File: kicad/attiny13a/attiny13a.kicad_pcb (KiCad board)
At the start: 2 copper layers, 28.2 x 17.8 mm, 6 parts, among them P1 CONN_01X04, P2 CONN_01X04, P3 CONN_01X06, U1 ATTINY13A-SSU

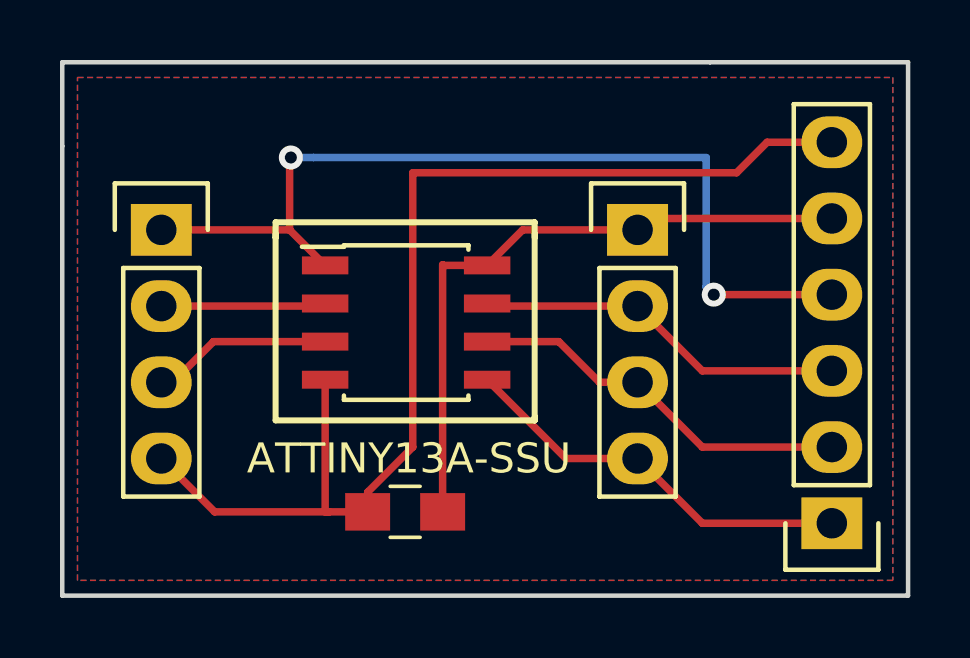
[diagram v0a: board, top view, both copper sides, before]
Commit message: make a better pcb
included sabor suggestions

1. Change vcc copper fill to GND fill
2. remove gnd traces
3. redraw vcc traces
4. move bypass capacitor close to Vcc/GND as much as possible.

Signed-off-by: Amitesh Singh <singh.amitesh@gmail.com>
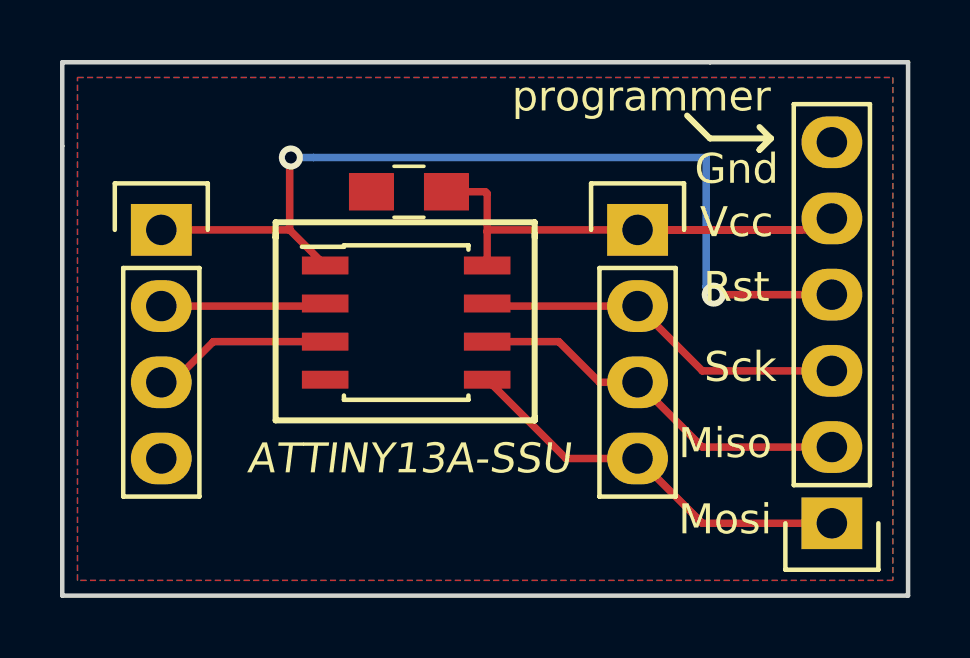
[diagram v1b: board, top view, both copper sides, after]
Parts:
- moved C1 10.7 mm to (131.2, 87.9)
- moved G*** 5.94 mm to (129.3, 96.5)
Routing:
- net GND: track 38.5 -> 0.00 mm
- net VCC: track 21.9 -> 20.9 mm
- added copper zone on F.Cu, net GND
- removed copper zone on F.Cu, net VCC
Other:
- board text added: "Gnd"
- board text added: "Miso"
- board text added: "Mosi"
- board text added: "Rst"
- board text added: "Sck"
- board text added: "Vcc"
- board text added: "programmer"

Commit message: change name to ISP
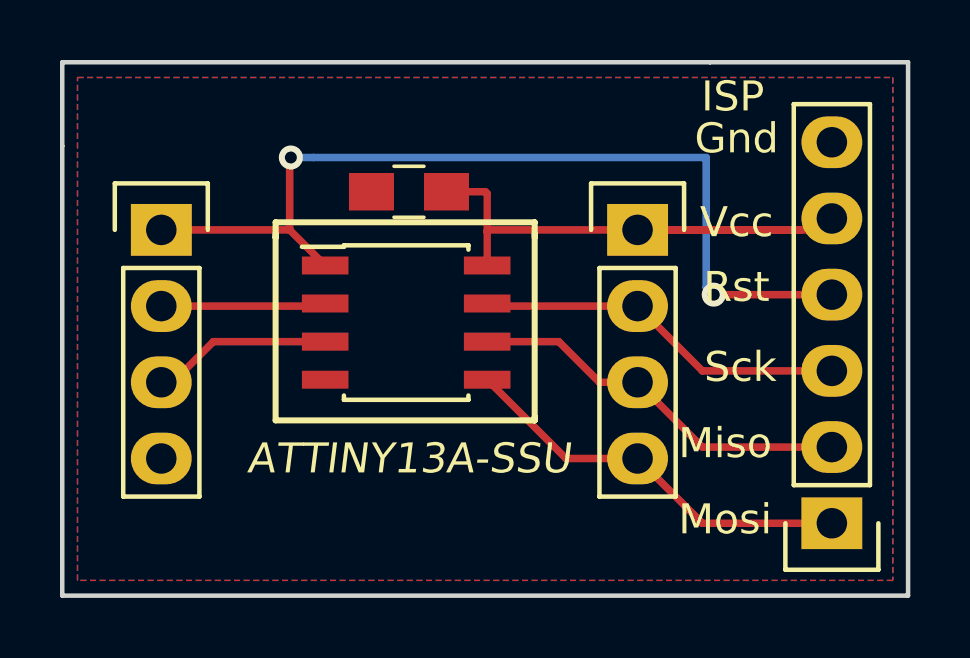
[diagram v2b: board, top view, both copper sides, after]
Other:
- board text added: "ISP"
- board text removed: "programmer"
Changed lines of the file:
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@@
     (links 16)
     (no_connects 0)
-    (area 119.558999 83.490999 147.903001 101.421001)
+    (area 119.558999 83.490999 149.8095 101.421001)
     (thickness 1.6)
-    (drawings 27)
+    (drawings 21)
     (tracks 38)
     (zones 0)
@@
       (effects (font (size 1 1) (thickness 0.15)))
     )
-    (fp_text value CONN_01X04 (at -1.905 2.413 360) (layer F.Fab) hide
+    (fp_text value CONN_01X04 (at -1.905 2.413) (layer F.Fab) hide
       (effects (font (size 1 1) (thickness 0.15)))
     )
@@
       (xy 4.318 -3.386667)) (layer B.SilkS) (width 0.01))
   )
-  (gr_text Gnd (at 142.113 87.122) (layer F.SilkS)
+  (gr_text Gnd (at 142.113 86.106) (layer F.SilkS)
     (effects (font (size 1 1) (thickness 0.2)))
   )
@@
     (effects (font (size 1 1) (thickness 0.2)))
   )
-  (gr_line (start 143.256 86.106) (end 142.875 85.725) (angle 90) (layer F.SilkS) (width 0.2))
-  (gr_line (start 142.875 86.487) (end 143.256 86.106) (angle 90) (layer F.SilkS) (width 0.2))
-  (gr_line (start 143.256 86.106) (end 142.875 86.487) (angle 90) (layer F.SilkS) (width 0.2))
-  (gr_line (start 143.129 86.106) (end 143.256 86.106) (angle 90) (layer F.SilkS) (width 0.2))
-  (gr_line (start 141.224 86.106) (end 143.129 86.106) (angle 90) (layer F.SilkS) (width 0.2))
-  (gr_line (start 140.462 85.344) (end 141.224 86.106) (angle 90) (layer F.SilkS) (width 0.2))
-  (gr_text programmer (at 138.938 84.709) (layer F.SilkS)
-    (effects (font (size 1 1) (thickness 0.2)))
-  )
+  (gr_text ISP (at 141.986 84.709) (layer F.SilkS)
+    (effects (font (size 1 1) (thickness 0.2)))
+  )

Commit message: make vcc track size bigger
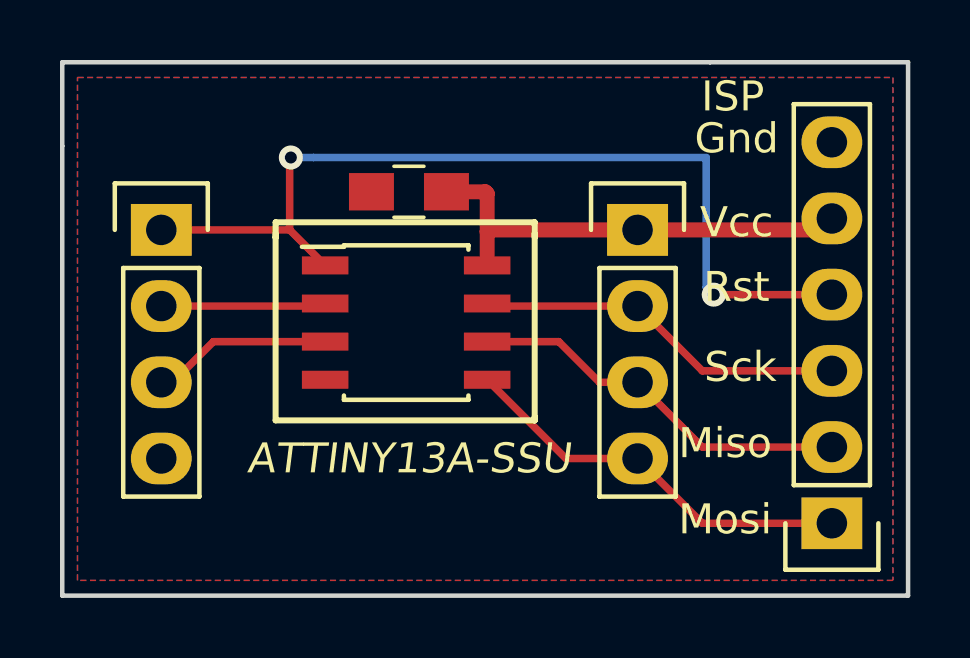
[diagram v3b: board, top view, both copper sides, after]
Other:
- net class power added: clearance 0.4, trace_width 0.5, via_dia 0.8, via_drill 0.4
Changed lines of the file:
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@@
     (add_net /pb4)
     (add_net /rst)
+  )
+  (net_class power ""
+    (clearance 0.4)
+    (trace_width 0.5)
+    (via_dia 0.8)
+    (via_drill 0.4)
+    (uvia_dia 0.3)
+    (uvia_drill 0.1)
     (add_net GND)
     (add_net VCC)
@@
   (gr_line (start 147.828 83.566) (end 147.828 101.346) (angle 90) (layer Edge.Cuts) (width 0.15))
   (gr_line (start 141.224 83.566) (end 147.828 83.566) (angle 90) (layer Edge.Cuts) (width 0.15))
-  (segment (start 133.798143 89.213857) (end 133.798143 87.943857) (width 0.25) (layer F.Cu) (net 2))
-  (segment (start 133.738286 87.884) (end 132.441 87.884) (width 0.25) (layer F.Cu) (net 2))
-  (segment (start 133.798143 87.943857) (end 133.738286 87.884) (width 0.25) (layer F.Cu) (net 2))
-  (segment (start 138.811 89.154) (end 144.907 89.154) (width 0.25) (layer F.Cu) (net 2))
+  (segment (start 133.798143 89.213857) (end 133.798143 87.943857) (width 0.5) (layer F.Cu) (net 2))
+  (segment (start 133.798143 87.943857) (end 133.738286 87.884) (width 0.5) (layer F.Cu) (net 2))
+  (segment (start 133.738286 87.884) (end 132.441 87.884) (width 0.5) (layer F.Cu) (net 2))
+  (segment (start 138.811 89.154) (end 144.907 89.154) (width 0.5) (layer F.Cu) (net 2))
   (segment (start 144.907 89.154) (end 145.288 88.773) (width 0.25) (layer F.Cu) (net 2))
   (segment (start 138.811 89.154) (end 144.272 89.154) (width 0.25) (layer F.Cu) (net 2))
-  (segment (start 138.811 89.154) (end 133.858 89.154) (width 0.25) (layer F.Cu) (net 2))
-  (segment (start 133.858 89.154) (end 133.798143 89.213857) (width 0.25) (layer F.Cu) (net 2))
-  (segment (start 133.798143 89.213857) (end 133.798143 90.3385) (width 0.25) (layer F.Cu) (net 2))
+  (segment (start 138.811 89.154) (end 133.858 89.154) (width 0.5) (layer F.Cu) (net 2))
+  (segment (start 133.858 89.154) (end 133.798143 89.213857) (width 0.5) (layer F.Cu) (net 2))
+  (segment (start 133.798143 89.213857) (end 133.798143 90.3385) (width 0.5) (layer F.Cu) (net 2))
   (segment (start 145.288 98.933) (end 140.97 98.933) (width 0.25) (layer F.Cu) (net 3))
   (segment (start 140.97 98.933) (end 138.811 96.774) (width 0.25) (layer F.Cu) (net 3))

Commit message: make vcc track size bigger
and also add logo of board.
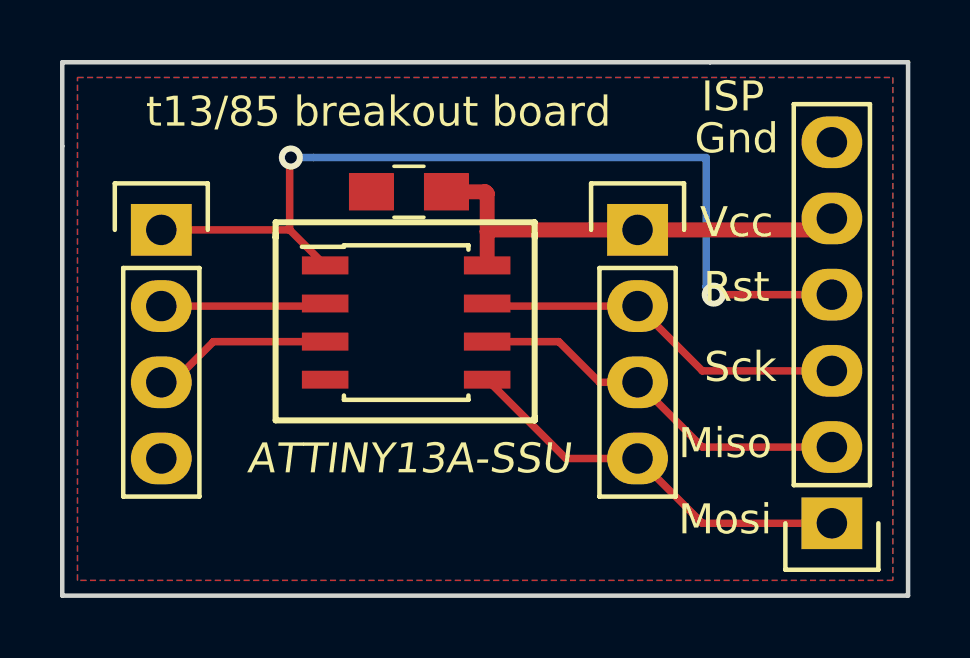
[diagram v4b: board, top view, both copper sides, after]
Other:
- board text added: "t13/85 breakout board"
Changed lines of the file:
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@@
     (links 16)
     (no_connects 0)
-    (area 119.558999 83.490999 149.8095 101.421001)
+    (area 119.558999 83.490999 147.903001 101.421001)
     (thickness 1.6)
-    (drawings 21)
+    (drawings 22)
     (tracks 38)
     (zones 0)
@@
       (xy 4.318 -3.386667)) (layer B.SilkS) (width 0.01))
   )
+  (gr_text "t13/85 breakout board" (at 130.175 85.217) (layer F.SilkS)
+    (effects (font (size 1 1) (thickness 0.2)))
+  )
   (gr_text Gnd (at 142.113 86.106) (layer F.SilkS)
